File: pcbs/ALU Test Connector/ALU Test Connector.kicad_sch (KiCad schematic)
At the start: 6 parts, among them J1 Conn_02x20_Odd_Even, J2 Conn_02x20_Odd_Even, J3 Conn_01x04

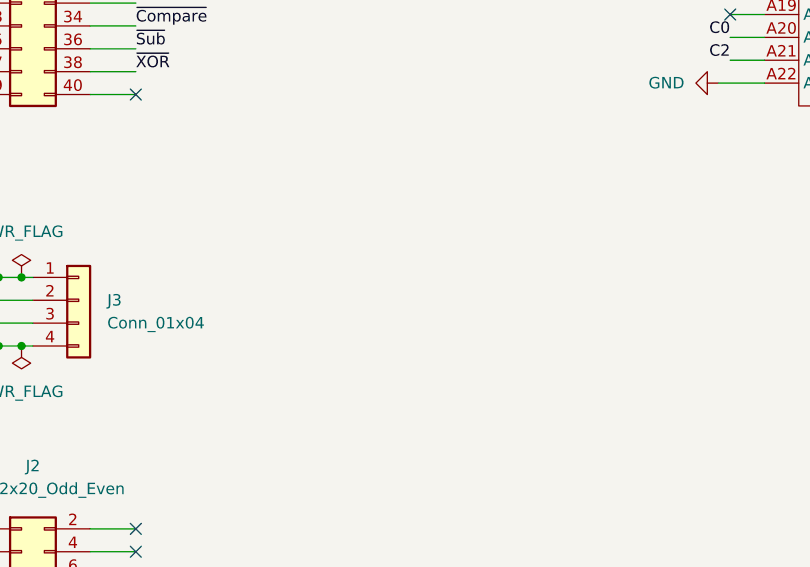
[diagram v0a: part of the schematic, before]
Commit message: Add alternative power connector
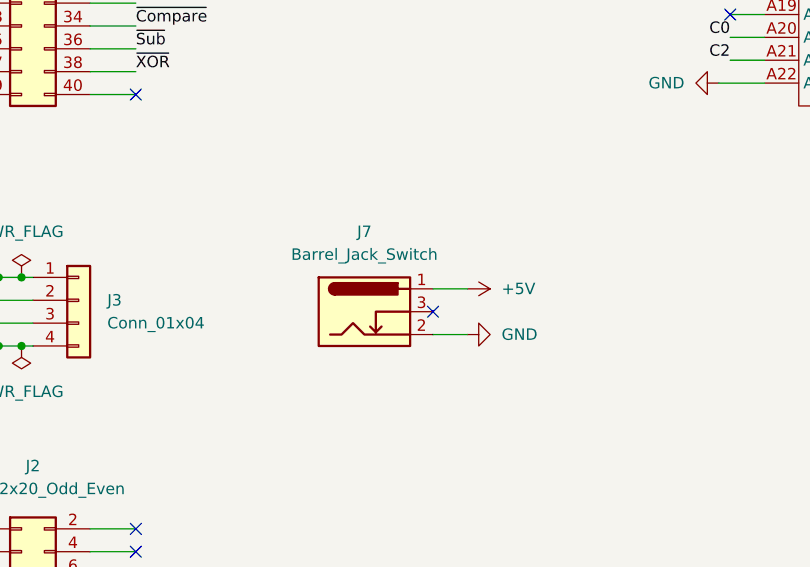
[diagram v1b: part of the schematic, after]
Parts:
- added J7: Barrel_Jack_Switch, Connector_BarrelJack:BarrelJack_Horizontal, symbol Connector:Barrel_Jack_Switch
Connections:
- net +5V: now also J7.1
- net GND: now also J7.2
- no-connect marks 68 -> 69
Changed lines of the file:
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@@
 	)
 	(no_connect
+		(at 90.17 105.41)
+	)
+	(no_connect
 		(at 152.4 49.53)
 	)
@@
 	(wire
 		(pts
+			(xy 90.17 107.95) (xy 93.98 107.95)
+		)
+		(stroke
+			(width 0)
+			(type default)
+		)
+	)
+	(wire
+		(pts
 			(xy 52.07 160.02) (xy 57.15 160.02)
 		)
@@
 	(wire
 		(pts
+			(xy 90.17 102.87) (xy 93.98 102.87)
+		)
+		(stroke
+			(width 0)
+			(type default)
+		)
+	)
+	(wire
+		(pts
 			(xy 123.19 64.77) (xy 127 64.77)
 		)
@@
 	)
 	(symbol
+		(lib_id "Connector:Barrel_Jack_Switch")
+		(at 82.55 105.41 0)
+		(unit 1)
+		(exclude_from_sim no)
+		(in_bom yes)
+		(on_board yes)
+		(dnp no)
+		(fields_autoplaced yes)
+		(property "Reference" "J7"
+			(at 82.55 96.52 0)
+			(effects
+				(font
+					(size 1.27 1.27)
+				)
+			)
+		)
+		(property "Value" "Barrel_Jack_Switch"
+			(at 82.55 99.06 0)
+			(effects
+				(font
+					(size 1.27 1.27)
+				)
+			)
+		)
+		(property "Footprint" "Connector_BarrelJack:BarrelJack_Horizontal"
+			(at 83.82 106.426 0)
+			(effects
+				(font
+					(size 1.27 1.27)
+				)
+				(hide yes)
+			)
+		)
+		(property "Datasheet" "~"
+			(at 83.82 106.426 0)
+			(effects
+				(font
+					(size 1.27 1.27)
+				)
+				(hide yes)
+			)
+		)
+		(property "Description" "DC Barrel Jack with an internal switch"
+			(at 82.55 105.41 0)
+			(effects
+				(font
+					(size 1.27 1.27)
+				)
+				(hide yes)
+			)
+		)
+		(pin "1"
+		)
+		(pin "2"
+		)
+		(pin "3"
+		)
+		(instances
+			(project ""
+				(path "/4fd220cc-43e4-4f22-8cf5-4ba061b6915f"
+					(reference "J7")
+					(unit 1)
+				)
+			)
+		)
+	)
+	(symbol
 		(lib_id "power:GND")
 		(at 182.88 77.47 270)
@@
 	)
 	(symbol
+		(lib_name "+5V_1")
+		(lib_id "power:+5V")
+		(at 93.98 102.87 270)
+		(unit 1)
+		(exclude_from_sim no)
+		(in_bom yes)
+		(on_board yes)
+		(dnp no)
+		(fields_autoplaced yes)
+		(property "Reference" "#PWR010"
+			(at 90.17 102.87 0)
+			(effects
+				(font
+					(size 1.27 1.27)
+				)
+				(hide yes)
+			)
+		)
+		(property "Value" "+5V"
+			(at 97.79 102.8699 90)
+			(effects
+				(font
+					(size 1.27 1.27)
+				)
+				(justify left)
+			)
+		)
+		(property "Footprint" ""
+			(at 93.98 102.87 0)
+			(effects
+				(font
+					(size 1.27 1.27)
+				)
+				(hide yes)
+			)
+		)
+		(property "Datasheet" ""
+			(at 93.98 102.87 0)
+			(effects
+				(font
+					(size 1.27 1.27)
+				)
+				(hide yes)
+			)
+		)
+		(property "Description" "Power symbol creates a global label with name \"+5V\""
+			(at 93.98 102.87 0)
+			(effects
+				(font
+					(size 1.27 1.27)
+				)
+				(hide yes)
+			)
+		)
+		(pin "1"
+		)
+		(instances
+			(project ""
+				(path "/4fd220cc-43e4-4f22-8cf5-4ba061b6915f"
+					(reference "#PWR010")
+					(unit 1)
+				)
+			)
+		)
+	)
+	(symbol
 		(lib_id "power:PWR_FLAG")
 		(at 44.45 109.22 180)
@@
 					(unit 1)
 				)
+			)
+		)
+	)
+	(symbol
+		(lib_name "GND_1")
+		(lib_id "power:GND")
+		(at 93.98 107.95 90)
+		(unit 1)
+		(exclude_from_sim no)
+		(in_bom yes)
+		(on_board yes)
+		(dnp no)
+		(fields_autoplaced yes)
+		(property "Reference" "#PWR011"
+			(at 100.33 107.95 0)
+			(effects
+				(font
+					(size 1.27 1.27)
+				)
+				(hide yes)
+			)
+		)
+		(property "Value" "GND"
+			(at 97.79 107.9499 90)
+			(effects
+				(font
+					(size 1.27 1.27)
+				)
+				(justify right)
+			)
+		)
+		(property "Footprint" ""
+			(at 93.98 107.95 0)
+			(effects
+				(font
+					(size 1.27 1.27)
+				)
+				(hide yes)
+			)
+		)
+		(property "Datasheet" ""
+			(at 93.98 107.95 0)
+			(effects
+				(font
+					(size 1.27 1.27)
+				)
+				(hide yes)
+			)
+		)
+		(property "Description" "Power symbol creates a global label with name \"GND\" , ground"
+			(at 93.98 107.95 0)
+			(effects
+				(font
+					(size 1.27 1.27)
+				)
+				(hide yes)
+			)
+		)
+		(pin "1"
+		)
+		(instances
+			(project ""
+				(path "/4fd220cc-43e4-4f22-8cf5-4ba061b6915f"
+					(reference "#PWR011")
+					(unit 1)
+				)
